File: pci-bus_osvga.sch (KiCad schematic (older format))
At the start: 1 part, among them J1 Bus_PCI_32bit_Universal_lrj

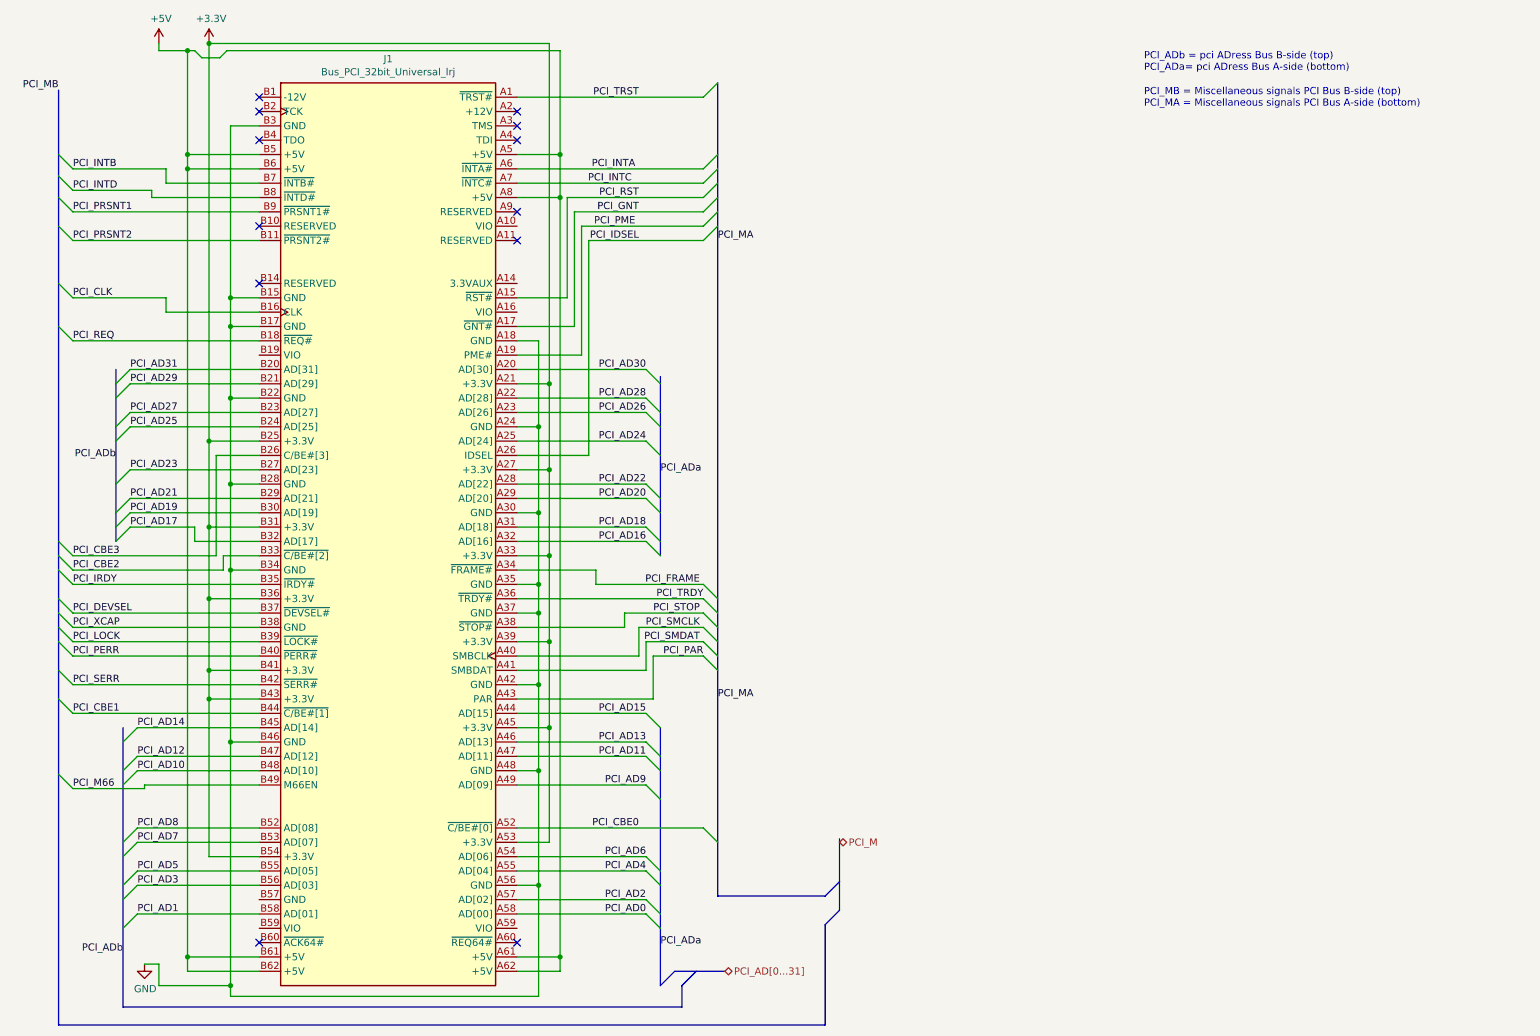
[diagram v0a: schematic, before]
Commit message: Add files via upload
Added Pull-up and pull-down resistors for JTAG and sysConfig connections.
Added pinheaders for FPGA-Configuration. (replacing edge-connector)
Combined the DVI+VGA and USB-C hierarchical sheets into one.
Assigned a dedicated sheet for the DAC.
Added 75 Ohm terminal-resistors to output of DAC.
Placed filtering-capacitors for DAC VAA.
Connected VGA ID-bits and DVI DDC together.
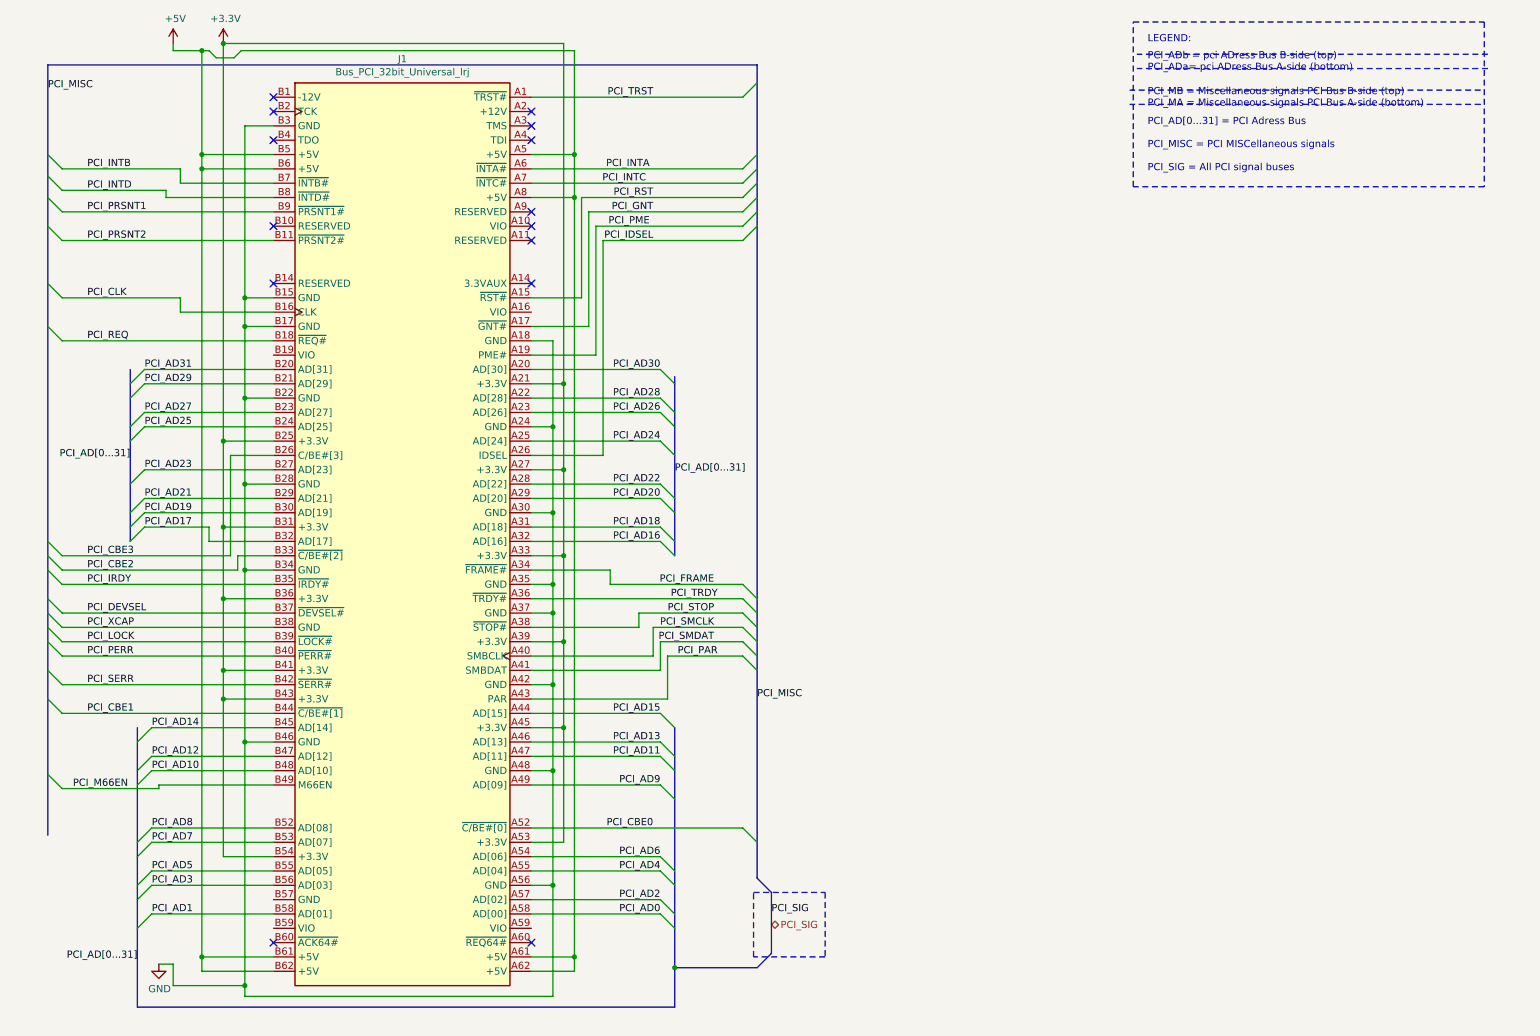
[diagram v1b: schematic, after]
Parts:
- J1: footprint Connector_PCBEdge:BUS_PCI_UNI_32-lrj -> Connector_PCBEdge:BUS_PCI_UNI_32-lrj2
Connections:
- net PCI_M66 renamed PCI_M66EN
- no-connect marks 12 -> 14
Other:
- note added: "LEGEND:"
- note added: "PCI_AD[0...31] = PCI Adress Bus\n\nPCI_MISC = PCI MISCellaneous signals\n\nPCI_SIG = All PCI signal buses"
- moved on the sheet: J1

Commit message: Add files via upload
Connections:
- net GND: now also J1.B57 (GND)
- no-connect marks 14 -> 17
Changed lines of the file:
@@
 $Descr A4 11693 8268
 encoding utf-8
-Sheet 9 9
+Sheet 8 9
 Title ""
 Date ""
@@
 Connection ~ 4300 6675
 Wire Wire Line
-	2150 5675 2150 7375
+	2150 5675 2150 6775
 Wire Wire Line
 	2000 6475 2350 6475
@@
 Text Label 5725 5375 0    50   ~ 0
 PCI_MISC
-Wire Bus Line
-	5725 950  5725 6625
-Wire Bus Line
-	775  950  775  6325
-Wire Bus Line
-	1400 5575 1400 7525
-Wire Bus Line
-	1350 3075 1350 4275
-Wire Bus Line
-	5150 3125 5150 4375
-Wire Bus Line
-	5150 5575 5150 7250
 Text Label 775  1125 0    50   ~ 0
 PCI_MISC
 Text Label 1050 1675 0    50   ~ 0
 PCI_INTB
+NoConn ~ 4150 2675
+NoConn ~ 4150 6975
+NoConn ~ 2350 6975
+Wire Wire Line
+	2350 6775 2150 6775
+Connection ~ 2150 6775
+Wire Wire Line
+	2150 6775 2150 7375
+Wire Bus Line
+	1350 3075 1350 4275
+Wire Bus Line
+	5150 3125 5150 4375
+Wire Bus Line
+	5150 5575 5150 7250
+Wire Bus Line
+	1400 5575 1400 7525
+Wire Bus Line
+	5725 950  5725 6625
+Wire Bus Line
+	775  950  775  6325
 $EndSCHEMATC
